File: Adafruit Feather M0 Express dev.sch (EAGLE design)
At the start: 37 parts, among them J2 AVR_SPI_PROG_3X2PTH, SW1 SPST_TACT-KMR2, U1 2MB Flash, U2 AP2112-3.3, U3 MCP73831T-2ACI/OT, X1 JSTPH, X2 32.768, X3 microUSB, X4 2x5 0.05" SWD

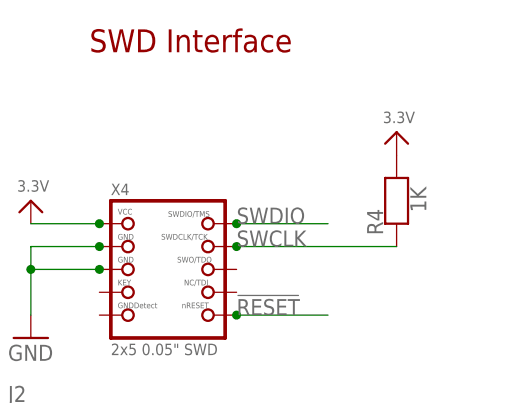
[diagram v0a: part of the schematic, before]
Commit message: fixed top angle DRCs. One bad overlap left
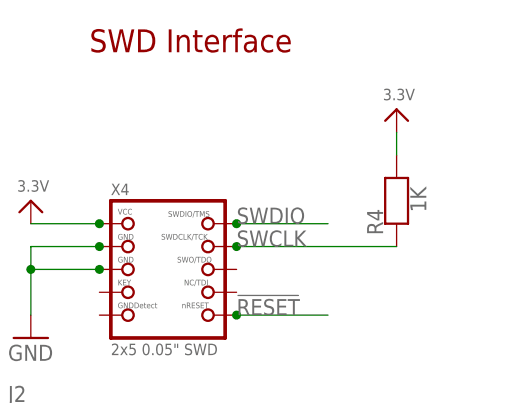
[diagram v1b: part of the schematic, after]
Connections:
- removed net 3.3V: R4.2
- net +3V3: now also R4.2
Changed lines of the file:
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@@
 <attribute name="VALUE" x="323.342" y="161.29" size="1.778" layer="96" rot="R90"/>
 </instance>
-<instance part="U$24" gate="G$1" x="320.04" y="170.18"/>
+<instance part="U$24" gate="G$1" x="320.04" y="172.72"/>
 <instance part="J2" gate="G$1" x="281.94" y="134.62"/>
 </instances>
@@
 <wire x1="297.18" y1="137.16" x2="292.1" y2="137.16" width="0.1524" layer="91"/>
 <pinref part="J2" gate="G$1" pin="2"/>
+</segment>
+<segment>
+<pinref part="R4" gate="G$1" pin="2"/>
+<pinref part="U$24" gate="G$1" pin="3.3V"/>
+<wire x1="320.04" y1="170.18" x2="320.04" y2="167.64" width="0.1524" layer="91"/>
 </segment>
 </net>
@@
 </segment>
 </net>
-<net name="3.3V" class="0">
-<segment>
-<pinref part="R4" gate="G$1" pin="2"/>
-<pinref part="U$24" gate="G$1" pin="3.3V"/>
-</segment>
-</net>

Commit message: fixed up silkscreen
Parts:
- removed U$35: FIDUCIAL"", microbuilder:FIDUCIAL""
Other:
- note added: "Developer mods by bsiepert"
- note added: "Original boards by Limor Fried & KTOWN"
- note added: "SPI Flash Header"
- note added: "SWD Header"
- note removed: "& bsiepert"
- note removed: "Limor Fried & KTOWN"
- note removed: "SWD Interface"
- moved on the sheet: J2
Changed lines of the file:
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@@
 <part name="GND10" library="supply1" deviceset="GND" device=""/>
 <part name="U$34" library="microbuilder" deviceset="FIDUCIAL" device="&quot;&quot;"/>
-<part name="U$35" library="microbuilder" deviceset="FIDUCIAL" device="&quot;&quot;"/>
 <part name="SW1" library="adafruit" deviceset="SPST_TACT" device="-KMR2"/>
 <part name="U$31" library="microbuilder" deviceset="MOUNTINGHOLE" device="2.5"/>
@@
 <text x="152.4" y="116.84" size="1.778" layer="91">Internal SPI on SERCOM 2</text>
 <wire x1="256.54" y1="124.46" x2="134.62" y2="124.46" width="0.1524" layer="94" style="shortdash"/>
-<text x="287.02" y="119.38" size="2.54" layer="94" font="vector">Limor Fried &amp; KTOWN</text>
-<text x="297.18" y="180.34" size="2.54" layer="94" ratio="15" align="center">SWD Interface</text>
-<text x="287.02" y="114.3" size="2.1844" layer="94">&amp; bsiepert</text>
+<text x="154.94" y="-5.08" size="2.54" layer="94" font="vector" ratio="10">Original boards by Limor Fried &amp; KTOWN</text>
+<text x="294.64" y="167.64" size="2.54" layer="94" ratio="15" align="center">SWD Header</text>
+<text x="165.1" y="-10.16" size="2.1844" layer="94" ratio="12">Developer mods by bsiepert</text>
+<text x="287.02" y="142.24" size="2.54" layer="94" ratio="15" align="center">SPI Flash Header</text>
 </plain>
 <instances>
@@
 <instance part="GND10" gate="1" x="246.38" y="48.26" rot="MR0"/>
 <instance part="U$34" gate="G$1" x="210.82" y="17.78"/>
-<instance part="U$35" gate="G$1" x="205.74" y="17.78"/>
 <instance part="SW1" gate="G$1" x="124.46" y="152.4" smashed="yes" rot="R270">
 <attribute name="NAME" x="121.92" y="158.75" size="1.778" layer="95"/>
@@
 </instance>
 <instance part="U$24" gate="G$1" x="320.04" y="172.72"/>
-<instance part="J2" gate="G$1" x="281.94" y="134.62"/>
+<instance part="J2" gate="G$1" x="287.02" y="132.08"/>
 </instances>
 <busses>
@@
 </segment>
 <segment>
-<wire x1="297.18" y1="132.08" x2="292.1" y2="132.08" width="0.1524" layer="91"/>
+<wire x1="302.26" y1="129.54" x2="297.18" y2="129.54" width="0.1524" layer="91"/>
 <pinref part="J2" gate="G$1" pin="6"/>
 </segment>
@@
 </segment>
 <segment>
-<wire x1="297.18" y1="137.16" x2="292.1" y2="137.16" width="0.1524" layer="91"/>
+<wire x1="302.26" y1="134.62" x2="297.18" y2="134.62" width="0.1524" layer="91"/>
 <pinref part="J2" gate="G$1" pin="2"/>
 </segment>
@@
 </segment>
 <segment>
-<wire x1="292.1" y1="134.62" x2="297.18" y2="134.62" width="0.1524" layer="91"/>
+<wire x1="297.18" y1="132.08" x2="302.26" y2="132.08" width="0.1524" layer="91"/>
 <pinref part="J2" gate="G$1" pin="4"/>
 </segment>
@@
 </segment>
 <segment>
-<wire x1="274.32" y1="134.62" x2="269.24" y2="134.62" width="0.1524" layer="91"/>
+<wire x1="279.4" y1="132.08" x2="274.32" y2="132.08" width="0.1524" layer="91"/>
 <pinref part="J2" gate="G$1" pin="3"/>
 </segment>
@@
 </segment>
 <segment>
-<wire x1="269.24" y1="137.16" x2="274.32" y2="137.16" width="0.1524" layer="91"/>
+<wire x1="274.32" y1="134.62" x2="279.4" y2="134.62" width="0.1524" layer="91"/>
 <pinref part="J2" gate="G$1" pin="1"/>
 </segment>
